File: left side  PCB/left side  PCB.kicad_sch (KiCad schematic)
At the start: 8 parts, among them U1 battery, U2 power_btr, U3 power_btr, U4 power_btr, U5 power_btr, U6 battery, U7 power_btr, U8 power_btr

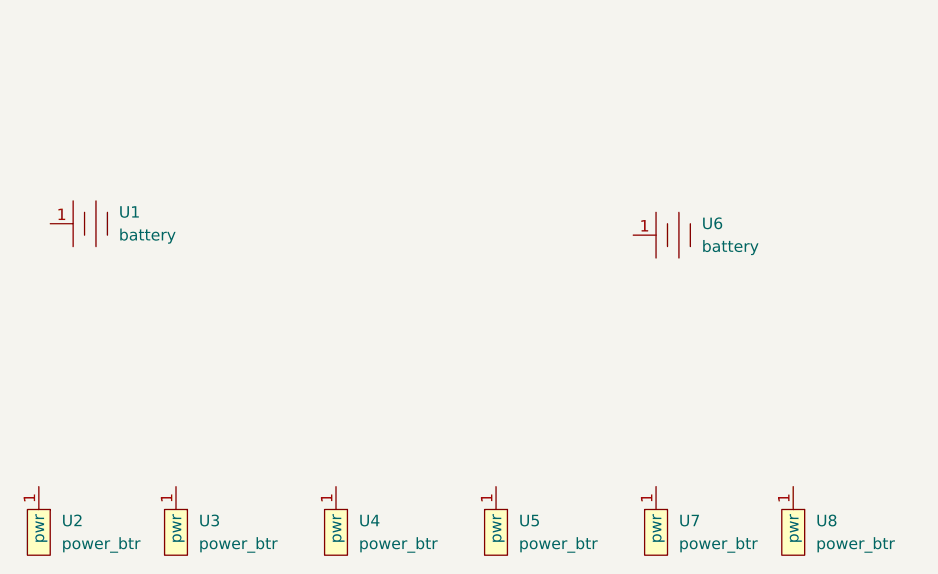
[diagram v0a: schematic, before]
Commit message: add led conn pcb
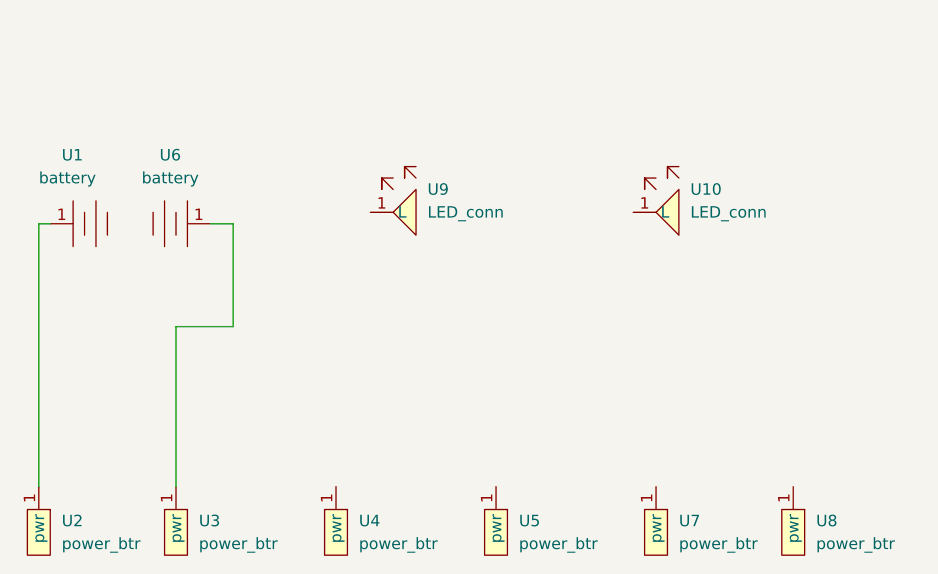
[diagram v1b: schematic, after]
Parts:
- added U10, U9: LED_conn, mother_conn_side:led_conn, symbol conn_mother_side:LED_conn
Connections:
- net at U6.1: now also U3.1 (pwr)
- net at U2.1 (pwr): now also U1.1
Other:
- moved on the sheet: U6
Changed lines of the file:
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@@
 (kicad_sch (version 20211123) (generator eeschema)
   (paper "A4")
+  (wire (pts (xy 102.87 88.9) (xy 96.52 88.9))
+    (stroke (width 0) (type default) (color 0 0 0 0))
+  )
+  (wire (pts (xy 81.28 106.68) (xy 81.28 77.47))
+    (stroke (width 0) (type default) (color 0 0 0 0))
+  )
+  (wire (pts (xy 96.52 88.9) (xy 96.52 106.68))
+    (stroke (width 0) (type default) (color 0 0 0 0))
+  )
+  (wire (pts (xy 100.33 77.47) (xy 102.87 77.47))
+    (stroke (width 0) (type default) (color 0 0 0 0))
+  )
+  (wire (pts (xy 81.28 77.47) (xy 82.55 77.47))
+    (stroke (width 0) (type default) (color 0 0 0 0))
+  )
+  (wire (pts (xy 102.87 77.47) (xy 102.87 88.9))
+    (stroke (width 0) (type default) (color 0 0 0 0))
+  )
   (symbol (lib_id "conn_mother_side:power_btr") (at 166.37 106.68 270) (unit 1)
     (in_bom yes) (on_board yes) (fields_autoplaced)
@@
     (pin "1")
   )
-  (symbol (lib_id "conn_mother_side:battery") (at 147.32 78.74 0) (unit 1)
-    (in_bom yes) (on_board yes) (fields_autoplaced)
-    (property "Reference" "U6" (id 0) (at 154.94 77.4699 0)
-      (effects (font (size 1.27 1.27)) (justify left))
-    )
-    (property "Value" "battery" (id 1) (at 154.94 80.0099 0)
-      (effects (font (size 1.27 1.27)) (justify left))
-    )
-    (property "Footprint" "mother_conn_side:btttr" (id 2) (at 147.32 78.74 0)
-      (effects (font (size 1.27 1.27)) hide)
-    )
-    (property "Datasheet" "" (id 3) (at 147.32 78.74 0)
+  (symbol (lib_id "conn_mother_side:battery") (at 100.33 77.47 180) (unit 1)
+    (in_bom yes) (on_board yes) (fields_autoplaced)
+    (property "Reference" "U6" (id 0) (at 95.885 69.85 0))
+    (property "Value" "battery" (id 1) (at 95.885 72.39 0))
+    (property "Footprint" "mother_conn_side:btttr" (id 2) (at 100.33 77.47 0)
+      (effects (font (size 1.27 1.27)) hide)
+    )
+    (property "Datasheet" "" (id 3) (at 100.33 77.47 0)
+      (effects (font (size 1.27 1.27)) hide)
+    )
+    (pin "1")
+  )
+  (symbol (lib_id "conn_mother_side:LED_conn") (at 118.11 76.2 0) (unit 1)
+    (in_bom yes) (on_board yes) (fields_autoplaced)
+    (property "Reference" "U9" (id 0) (at 124.46 73.6599 0)
+      (effects (font (size 1.27 1.27)) (justify left))
+    )
+    (property "Value" "LED_conn" (id 1) (at 124.46 76.1999 0)
+      (effects (font (size 1.27 1.27)) (justify left))
+    )
+    (property "Footprint" "mother_conn_side:led_conn" (id 2) (at 118.11 76.2 0)
+      (effects (font (size 1.27 1.27)) hide)
+    )
+    (property "Datasheet" "" (id 3) (at 118.11 76.2 0)
       (effects (font (size 1.27 1.27)) hide)
     )
@@
     (pin "1")
   )
+  (symbol (lib_id "conn_mother_side:LED_conn") (at 147.32 76.2 0) (unit 1)
+    (in_bom yes) (on_board yes) (fields_autoplaced)
+    (property "Reference" "U10" (id 0) (at 153.67 73.6599 0)
+      (effects (font (size 1.27 1.27)) (justify left))
+    )
+    (property "Value" "LED_conn" (id 1) (at 153.67 76.1999 0)
+      (effects (font (size 1.27 1.27)) (justify left))
+    )
+    (property "Footprint" "mother_conn_side:led_conn" (id 2) (at 147.32 76.2 0)
+      (effects (font (size 1.27 1.27)) hide)
+    )
+    (property "Datasheet" "" (id 3) (at 147.32 76.2 0)
+      (effects (font (size 1.27 1.27)) hide)
+    )
+    (pin "1")
+  )
   (symbol (lib_id "conn_mother_side:battery") (at 82.55 77.47 0) (unit 1)
-    (in_bom yes) (on_board yes) (fields_autoplaced)
-    (property "Reference" "U1" (id 0) (at 90.17 76.1999 0)
-      (effects (font (size 1.27 1.27)) (justify left))
-    )
-    (property "Value" "battery" (id 1) (at 90.17 78.7399 0)
+    (in_bom yes) (on_board yes)
+    (property "Reference" "U1" (id 0) (at 83.82 69.85 0)
+      (effects (font (size 1.27 1.27)) (justify left))
+    )
+    (property "Value" "battery" (id 1) (at 81.28 72.39 0)
       (effects (font (size 1.27 1.27)) (justify left))
     )
@@
       (reference "U8") (unit 1) (value "power_btr") (footprint "mother_conn_side:conn_side")
     )
-  )
+    (path "/5723b6f5-fa91-4114-bd90-1e066b938b1e"
+      (reference "U9") (unit 1) (value "LED_conn") (footprint "mother_conn_side:led_conn")
+    )
+    (path "/e806bb37-412c-48ae-9973-024e0e813d16"
+      (reference "U10") (unit 1) (value "LED_conn") (footprint "mother_conn_side:led_conn")
+    )
+  )

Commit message: correct conn led
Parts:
- added Q1, Q2: BSS83P, Package_TO_SOT_SMD:SOT-23, symbol Transistor_FET:BSS83P
- added R1, R2: 30, Resistor_SMD:R_0603_1608Metric_Pad0.98x0.95mm_HandSolder, symbol Device:R
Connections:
- net at U9.1 (L): now also R1.1
- net at U4.1 (pwr): now also Q1.1 (G)
- net at U5.1 (pwr): now also Q2.1 (G)
- net at U7.1 (pwr): now also Q1.2 (S), Q2.2 (S)
- net at U10.1 (L): now also R2.1
- new net: Q2.3 (D), R2.2
- new net: Q1.3 (D), R1.2
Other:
- moved on the sheet: U10, U5, U9
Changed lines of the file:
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@@
 (kicad_sch (version 20211123) (generator eeschema)
   (paper "A4")
+  (junction (at 142.24 101.6) (diameter 0) (color 0 0 0 0)
+  )
+  (wire (pts (xy 149.86 106.68) (xy 149.86 101.6))
+    (stroke (width 0) (type default) (color 0 0 0 0))
+  )
   (wire (pts (xy 102.87 88.9) (xy 96.52 88.9))
     (stroke (width 0) (type default) (color 0 0 0 0))
@@
     (stroke (width 0) (type default) (color 0 0 0 0))
   )
+  (wire (pts (xy 134.62 91.44) (xy 134.62 106.68))
+    (stroke (width 0) (type default) (color 0 0 0 0))
+  )
   (wire (pts (xy 96.52 88.9) (xy 96.52 106.68))
     (stroke (width 0) (type default) (color 0 0 0 0))
   )
+  (wire (pts (xy 121.92 59.69) (xy 121.92 69.85))
+    (stroke (width 0) (type default) (color 0 0 0 0))
+  )
+  (wire (pts (xy 149.86 101.6) (xy 142.24 101.6))
+    (stroke (width 0) (type default) (color 0 0 0 0))
+  )
+  (wire (pts (xy 121.92 96.52) (xy 121.92 101.6))
+    (stroke (width 0) (type default) (color 0 0 0 0))
+  )
+  (wire (pts (xy 142.24 101.6) (xy 121.92 101.6))
+    (stroke (width 0) (type default) (color 0 0 0 0))
+  )
   (wire (pts (xy 100.33 77.47) (xy 102.87 77.47))
     (stroke (width 0) (type default) (color 0 0 0 0))
@@
     (stroke (width 0) (type default) (color 0 0 0 0))
   )
+  (wire (pts (xy 121.92 77.47) (xy 121.92 86.36))
+    (stroke (width 0) (type default) (color 0 0 0 0))
+  )
+  (wire (pts (xy 142.24 96.52) (xy 142.24 101.6))
+    (stroke (width 0) (type default) (color 0 0 0 0))
+  )
+  (wire (pts (xy 142.24 77.47) (xy 142.24 86.36))
+    (stroke (width 0) (type default) (color 0 0 0 0))
+  )
   (wire (pts (xy 102.87 77.47) (xy 102.87 88.9))
     (stroke (width 0) (type default) (color 0 0 0 0))
   )
+  (wire (pts (xy 142.24 59.69) (xy 142.24 69.85))
+    (stroke (width 0) (type default) (color 0 0 0 0))
+  )
+  (wire (pts (xy 114.3 91.44) (xy 114.3 106.68))
+    (stroke (width 0) (type default) (color 0 0 0 0))
+  )
+  (symbol (lib_id "Transistor_FET:BSS83P") (at 139.7 91.44 0) (unit 1)
+    (in_bom yes) (on_board yes) (fields_autoplaced)
+    (property "Reference" "Q2" (id 0) (at 146.05 90.1699 0)
+      (effects (font (size 1.27 1.27)) (justify left))
+    )
+    (property "Value" "BSS83P" (id 1) (at 146.05 92.7099 0)
+      (effects (font (size 1.27 1.27)) (justify left))
+    )
+    (property "Footprint" "Package_TO_SOT_SMD:SOT-23" (id 2) (at 144.78 93.345 0)
+      (effects (font (size 1.27 1.27) italic) (justify left) hide)
+    )
+    (property "Datasheet" "http://www.farnell.com/datasheets/1835997.pdf" (id 3) (at 139.7 91.44 0)
+      (effects (font (size 1.27 1.27)) (justify left) hide)
+    )
+    (pin "1")
+    (pin "2")
+    (pin "3")
+  )
   (symbol (lib_id "conn_mother_side:power_btr") (at 166.37 106.68 270) (unit 1)
     (in_bom yes) (on_board yes) (fields_autoplaced)
@@
     )
     (pin "1")
+  )
+  (symbol (lib_id "Device:R") (at 142.24 73.66 0) (unit 1)
+    (in_bom yes) (on_board yes) (fields_autoplaced)
+    (property "Reference" "R2" (id 0) (at 144.78 72.3899 0)
+      (effects (font (size 1.27 1.27)) (justify left))
+    )
+    (property "Value" "30" (id 1) (at 144.78 74.9299 0)
+      (effects (font (size 1.27 1.27)) (justify left))
+    )
+    (property "Footprint" "Resistor_SMD:R_0603_1608Metric_Pad0.98x0.95mm_HandSolder" (id 2) (at 140.462 73.66 90)
+      (effects (font (size 1.27 1.27)) hide)
+    )
+    (property "Datasheet" "~" (id 3) (at 142.24 73.66 0)
+      (effects (font (size 1.27 1.27)) hide)
+    )
+    (pin "1")
+    (pin "2")
   )
   (symbol (lib_id "conn_mother_side:battery") (at 100.33 77.47 180) (unit 1)
@@
     (pin "1")
   )
-  (symbol (lib_id "conn_mother_side:LED_conn") (at 118.11 76.2 0) (unit 1)
-    (in_bom yes) (on_board yes) (fields_autoplaced)
-    (property "Reference" "U9" (id 0) (at 124.46 73.6599 0)
-      (effects (font (size 1.27 1.27)) (justify left))
-    )
-    (property "Value" "LED_conn" (id 1) (at 124.46 76.1999 0)
-      (effects (font (size 1.27 1.27)) (justify left))
-    )
-    (property "Footprint" "mother_conn_side:led_conn" (id 2) (at 118.11 76.2 0)
-      (effects (font (size 1.27 1.27)) hide)
-    )
-    (property "Datasheet" "" (id 3) (at 118.11 76.2 0)
+  (symbol (lib_id "conn_mother_side:LED_conn") (at 121.92 59.69 0) (unit 1)
+    (in_bom yes) (on_board yes) (fields_autoplaced)
+    (property "Reference" "U9" (id 0) (at 128.27 57.1499 0)
+      (effects (font (size 1.27 1.27)) (justify left))
+    )
+    (property "Value" "LED_conn" (id 1) (at 128.27 59.6899 0)
+      (effects (font (size 1.27 1.27)) (justify left))
+    )
+    (property "Footprint" "mother_conn_side:led_conn" (id 2) (at 121.92 59.69 0)
+      (effects (font (size 1.27 1.27)) hide)
+    )
+    (property "Datasheet" "" (id 3) (at 121.92 59.69 0)
       (effects (font (size 1.27 1.27)) hide)
     )
@@
     (pin "1")
   )
-  (symbol (lib_id "conn_mother_side:power_btr") (at 133.35 106.68 270) (unit 1)
-    (in_bom yes) (on_board yes) (fields_autoplaced)
-    (property "Reference" "U5" (id 0) (at 134.62 110.4899 90)
-      (effects (font (size 1.27 1.27)) (justify left))
-    )
-    (property "Value" "power_btr" (id 1) (at 134.62 113.0299 90)
-      (effects (font (size 1.27 1.27)) (justify left))
-    )
-    (property "Footprint" "mother_conn_side:conn_side" (id 2) (at 133.35 106.68 0)
-      (effects (font (size 1.27 1.27)) hide)
-    )
-    (property "Datasheet" "" (id 3) (at 133.35 106.68 0)
-      (effects (font (size 1.27 1.27)) hide)
-    )
-    (pin "1")
+  (symbol (lib_id "conn_mother_side:power_btr") (at 135.89 106.68 270) (unit 1)
+    (in_bom yes) (on_board yes) (fields_autoplaced)
+    (property "Reference" "U5" (id 0) (at 137.16 110.4899 90)
+      (effects (font (size 1.27 1.27)) (justify left))
+    )
+    (property "Value" "power_btr" (id 1) (at 137.16 113.0299 90)
+      (effects (font (size 1.27 1.27)) (justify left))
+    )
+    (property "Footprint" "mother_conn_side:conn_side" (id 2) (at 135.89 106.68 0)
+      (effects (font (size 1.27 1.27)) hide)
+    )
+    (property "Datasheet" "" (id 3) (at 135.89 106.68 0)
+      (effects (font (size 1.27 1.27)) hide)
+    )
+    (pin "1")
+  )
+  (symbol (lib_id "Device:R") (at 121.92 73.66 0) (unit 1)
+    (in_bom yes) (on_board yes) (fields_autoplaced)
+    (property "Reference" "R1" (id 0) (at 124.46 72.3899 0)
+      (effects (font (size 1.27 1.27)) (justify left))
+    )
+    (property "Value" "30" (id 1) (at 124.46 74.9299 0)
+      (effects (font (size 1.27 1.27)) (justify left))
+    )
+    (property "Footprint" "Resistor_SMD:R_0603_1608Metric_Pad0.98x0.95mm_HandSolder" (id 2) (at 120.142 73.66 90)
+      (effects (font (size 1.27 1.27)) hide)
+    )
+    (property "Datasheet" "~" (id 3) (at 121.92 73.66 0)
+      (effects (font (size 1.27 1.27)) hide)
+    )
+    (pin "1")
+    (pin "2")
   )
   (symbol (lib_id "conn_mother_side:power_btr") (at 151.13 106.68 270) (unit 1)
@@
     (pin "1")
   )
-  (symbol (lib_id "conn_mother_side:LED_conn") (at 147.32 76.2 0) (unit 1)
-    (in_bom yes) (on_board yes) (fields_autoplaced)
-    (property "Reference" "U10" (id 0) (at 153.67 73.6599 0)
-      (effects (font (size 1.27 1.27)) (justify left))
-    )
-    (property "Value" "LED_conn" (id 1) (at 153.67 76.1999 0)
-      (effects (font (size 1.27 1.27)) (justify left))
-    )
-    (property "Footprint" "mother_conn_side:led_conn" (id 2) (at 147.32 76.2 0)
-      (effects (font (size 1.27 1.27)) hide)
-    )
-    (property "Datasheet" "" (id 3) (at 147.32 76.2 0)
+  (symbol (lib_id "Transistor_FET:BSS83P") (at 119.38 91.44 0) (unit 1)
+    (in_bom yes) (on_board yes) (fields_autoplaced)
+    (property "Reference" "Q1" (id 0) (at 125.73 90.1699 0)
+      (effects (font (size 1.27 1.27)) (justify left))
+    )
+    (property "Value" "BSS83P" (id 1) (at 125.73 92.7099 0)
+      (effects (font (size 1.27 1.27)) (justify left))
+    )
+    (property "Footprint" "Package_TO_SOT_SMD:SOT-23" (id 2) (at 124.46 93.345 0)
+      (effects (font (size 1.27 1.27) italic) (justify left) hide)
+    )
+    (property "Datasheet" "http://www.farnell.com/datasheets/1835997.pdf" (id 3) (at 119.38 91.44 0)
+      (effects (font (size 1.27 1.27)) (justify left) hide)
+    )
+    (pin "1")
+    (pin "2")
+    (pin "3")
+  )
+  (symbol (lib_id "conn_mother_side:LED_conn") (at 142.24 59.69 0) (unit 1)
+    (in_bom yes) (on_board yes) (fields_autoplaced)
+    (property "Reference" "U10" (id 0) (at 148.59 57.1499 0)
+      (effects (font (size 1.27 1.27)) (justify left))
+    )
+    (property "Value" "LED_conn" (id 1) (at 148.59 59.6899 0)
+      (effects (font (size 1.27 1.27)) (justify left))
+    )
+    (property "Footprint" "mother_conn_side:led_conn" (id 2) (at 142.24 59.69 0)
+      (effects (font (size 1.27 1.27)) hide)
+    )
+    (property "Datasheet" "" (id 3) (at 142.24 59.69 0)
       (effects (font (size 1.27 1.27)) hide)
     )
@@
   )
   (symbol_instances
+    (path "/df83f395-2d18-47e2-a370-952ca41c2b3a"
+      (reference "Q1") (unit 1) (value "BSS83P") (footprint "Package_TO_SOT_SMD:SOT-23")
+    )
+    (path "/05c66f7d-5ec1-4b7f-80d5-ea1eb396392f"
+      (reference "Q2") (unit 1) (value "BSS83P") (footprint "Package_TO_SOT_SMD:SOT-23")
+    )
+    (path "/ad9c236e-bc99-4c14-a98d-6497c553eb20"
+      (reference "R1") (unit 1) (value "30") (footprint "Resistor_SMD:R_0603_1608Metric_Pad0.98x0.95mm_HandSolder")
+    )
+    (path "/3edeed73-8ebc-490d-a770-d1eec67e7668"
+      (reference "R2") (unit 1) (value "30") (footprint "Resistor_SMD:R_0603_1608Metric_Pad0.98x0.95mm_HandSolder")
+    )
     (path "/f851ba2e-9529-4507-834a-7717863796ac"
       (reference "U1") (unit 1) (value "battery") (footprint "mother_conn_side:btttr")
